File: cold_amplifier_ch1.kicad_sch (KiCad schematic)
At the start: 28 parts, among them J2 T1M-03-F-SV-L, J3 T1M-03-F-SV-L, J4 T1M-03-F-SV-L, J5 T1M-03-F-SV-L

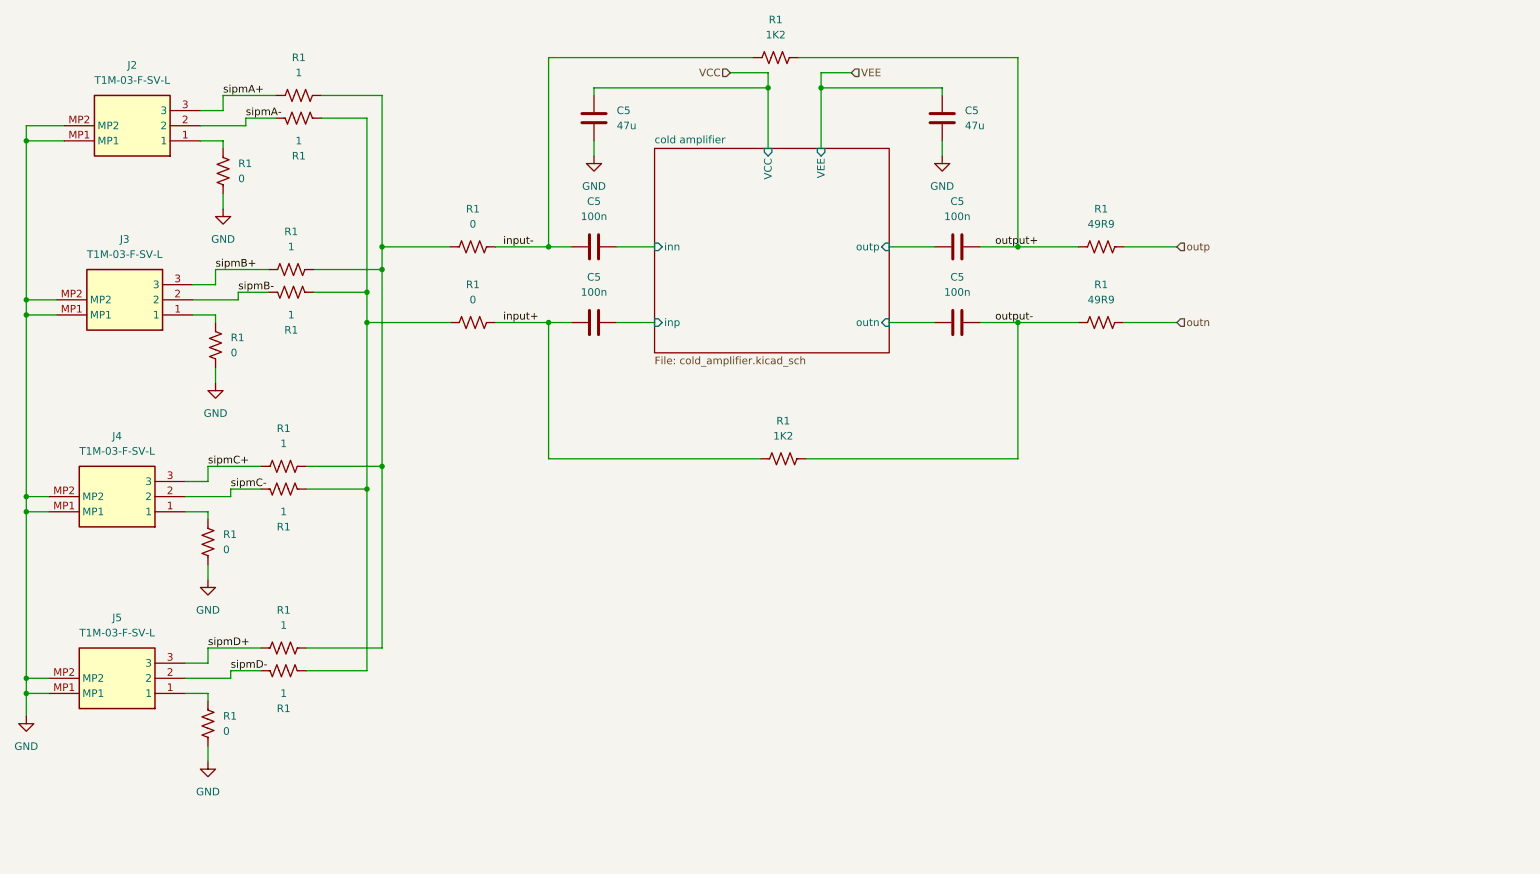
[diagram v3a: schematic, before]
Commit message: completed BOM list; replaced 47u with 33u capacitor
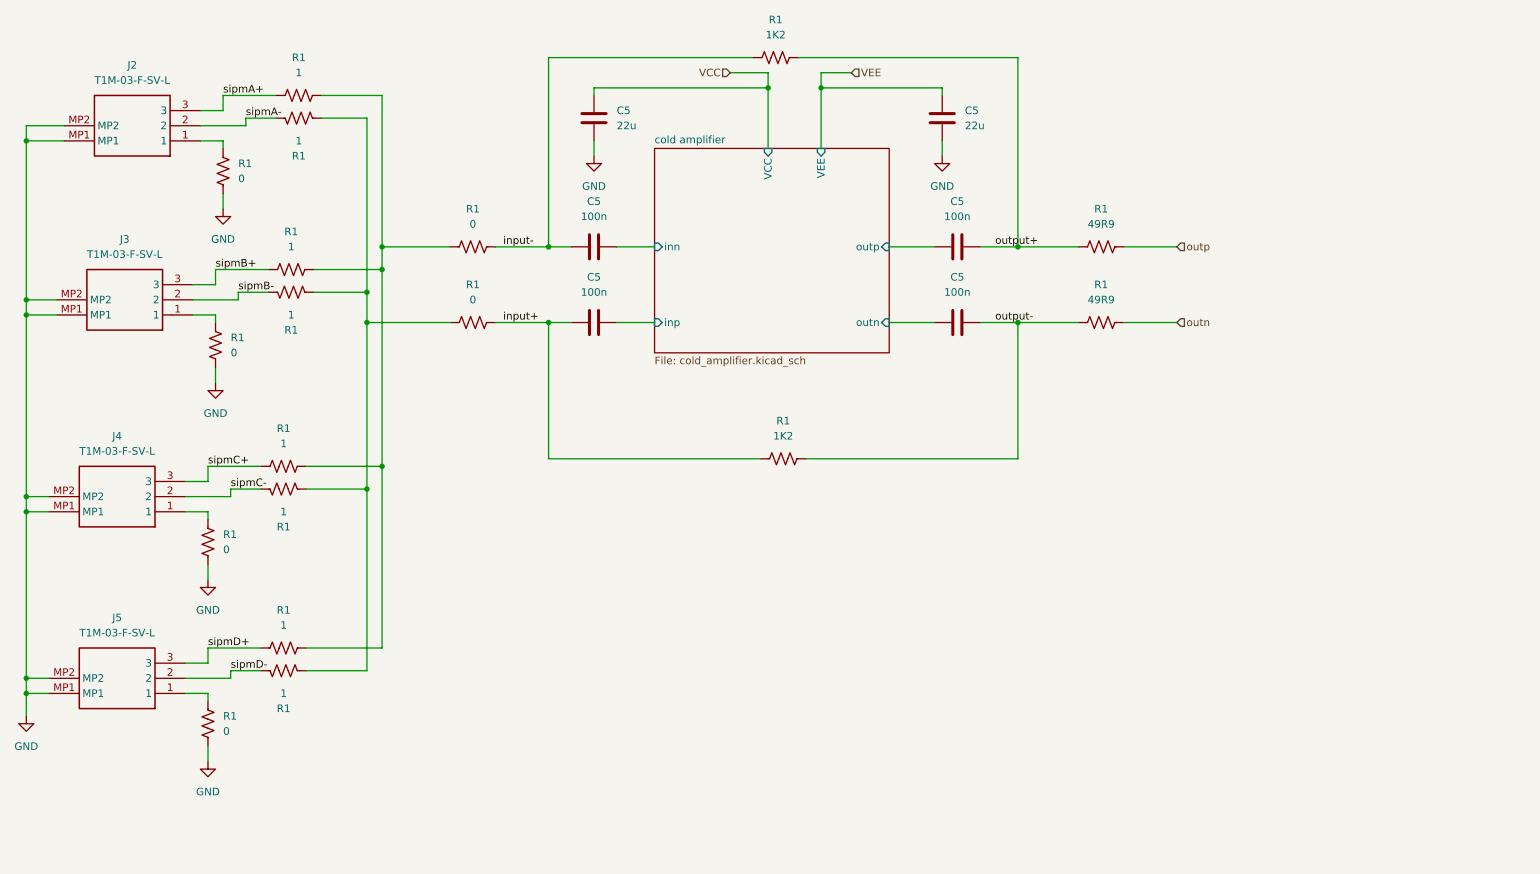
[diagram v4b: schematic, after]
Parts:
- C5: value 47u -> 22u; Digikey Part Number (none) -> 490-GRM31C5C1H224JE02LCT-ND; Manufacturer (none) -> Murata Electronics; Part Number (none) -> GRM31C5C1H224JE02L
- J2: Digikey Part SAM15301CT-ND -> (none); Digikey Part Number (none) -> SAM15301CT-ND; Height 5.5 -> (none); Manufacturer (none) -> SAMTEC; Manufacturer Name SAMTEC -> (none); Manufacturer_Name SAMTEC -> (none); Manufacturer_Part_Number T1M-03-F-SV-L -> (none); Mouser Part Number 200-T1M03FSVL -> (none); Mouser Price/Stock https://www.mouser.co.uk/ProductDetail/Samtec/T1M-03-F-SV-L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 -> (none)
- J3, J4, J5: Description  Connector Header Surface Mount 3 position 0.039" (1.00mm) -> (none); Height 5.5 -> (none); Manufacturer (none) -> SAMTEC; Manufacturer Name SAMTEC -> (none); Manufacturer_Name SAMTEC -> (none); Manufacturer_Part_Number T1M-03-F-SV-L -> (none); Mouser Part Number 200-T1M03FSVL -> (none); Mouser Price/Stock https://www.mouser.co.uk/ProductDetail/Samtec/T1M-03-F-SV-L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 -> (none)
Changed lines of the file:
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@@
       (effects (font (size 1.27 1.27)) (justify left top) hide)
     )
-    (property "Datasheet" "http://suddendocs.samtec.com/prints/t1m-xx-x-sv-l-x-mkt.pdf" (at 25.4 -28.55 0)
-      (effects (font (size 1.27 1.27)) (justify left top) hide)
-    )
-    (property "Height" "5.5" (at 25.4 -228.55 0)
-      (effects (font (size 1.27 1.27)) (justify left top) hide)
-    )
-    (property "Mouser Part Number" "200-T1M03FSVL" (at 25.4 -328.55 0)
-      (effects (font (size 1.27 1.27)) (justify left top) hide)
-    )
-    (property "Mouser Price/Stock" "https://www.mouser.co.uk/ProductDetail/Samtec/T1M-03-F-SV-L?qs=PB6%2FjmICvI1GeF9c7xI%252BBQ%3D%3D" (at 25.4 -428.55 0)
-      (effects (font (size 1.27 1.27)) (justify left top) hide)
-    )
-    (property "Manufacturer_Name" "SAMTEC" (at 25.4 -528.55 0)
-      (effects (font (size 1.27 1.27)) (justify left top) hide)
-    )
-    (property "Manufacturer_Part_Number" "T1M-03-F-SV-L" (at 25.4 -628.55 0)
-      (effects (font (size 1.27 1.27)) (justify left top) hide)
-    )
-    (property "Manufacturer Name" "SAMTEC" (at 25.4 -528.55 0)
+    (property "Datasheet" "" (at 25.4 -28.55 0)
+      (effects (font (size 1.27 1.27)) (justify left top) hide)
+    )
+    (property "Manufacturer" "SAMTEC" (at 25.4 -528.55 0)
       (effects (font (size 1.27 1.27)) (justify left top) hide)
     )
@@
     )
     (property "Digikey Part Number" "SAM15301CT-ND" (at 33.02 157.48 0)
-      (effects (font (size 1.27 1.27)) hide)
-    )
-    (property "Description " "Connector Header Surface Mount 3 position 0.039\" (1.00mm)" (at 41.91 176.53 0)
       (effects (font (size 1.27 1.27)) hide)
     )
@@
       (effects (font (size 1.27 1.27)) (justify left top) hide)
     )
-    (property "Datasheet" "http://suddendocs.samtec.com/prints/t1m-xx-x-sv-l-x-mkt.pdf" (at 25.4 -59.03 0)
-      (effects (font (size 1.27 1.27)) (justify left top) hide)
-    )
-    (property "Height" "5.5" (at 25.4 -259.03 0)
-      (effects (font (size 1.27 1.27)) (justify left top) hide)
-    )
-    (property "Mouser Part Number" "200-T1M03FSVL" (at 25.4 -359.03 0)
-      (effects (font (size 1.27 1.27)) (justify left top) hide)
-    )
-    (property "Mouser Price/Stock" "https://www.mouser.co.uk/ProductDetail/Samtec/T1M-03-F-SV-L?qs=PB6%2FjmICvI1GeF9c7xI%252BBQ%3D%3D" (at 25.4 -459.03 0)
-      (effects (font (size 1.27 1.27)) (justify left top) hide)
-    )
-    (property "Manufacturer_Name" "SAMTEC" (at 25.4 -559.03 0)
-      (effects (font (size 1.27 1.27)) (justify left top) hide)
-    )
-    (property "Manufacturer_Part_Number" "T1M-03-F-SV-L" (at 25.4 -659.03 0)
-      (effects (font (size 1.27 1.27)) (justify left top) hide)
-    )
-    (property "Manufacturer Name" "SAMTEC" (at 25.4 -559.03 0)
+    (property "Datasheet" "" (at 25.4 -59.03 0)
+      (effects (font (size 1.27 1.27)) (justify left top) hide)
+    )
+    (property "Manufacturer" "SAMTEC" (at 25.4 -559.03 0)
       (effects (font (size 1.27 1.27)) (justify left top) hide)
     )
@@
     )
     (property "Digikey Part Number" "SAM15301CT-ND" (at 33.02 127 0)
-      (effects (font (size 1.27 1.27)) hide)
-    )
-    (property "Description " "Connector Header Surface Mount 3 position 0.039\" (1.00mm)" (at 41.91 146.05 0)
       (effects (font (size 1.27 1.27)) hide)
     )
@@
       (effects (font (size 1.27 1.27)) (justify left top) hide)
     )
-    (property "Datasheet" "http://suddendocs.samtec.com/prints/t1m-xx-x-sv-l-x-mkt.pdf" (at 26.67 -92.05 0)
-      (effects (font (size 1.27 1.27)) (justify left top) hide)
-    )
-    (property "Height" "5.5" (at 26.67 -292.05 0)
-      (effects (font (size 1.27 1.27)) (justify left top) hide)
-    )
-    (property "Mouser Part Number" "200-T1M03FSVL" (at 26.67 -392.05 0)
-      (effects (font (size 1.27 1.27)) (justify left top) hide)
-    )
-    (property "Mouser Price/Stock" "https://www.mouser.co.uk/ProductDetail/Samtec/T1M-03-F-SV-L?qs=PB6%2FjmICvI1GeF9c7xI%252BBQ%3D%3D" (at 26.67 -492.05 0)
-      (effects (font (size 1.27 1.27)) (justify left top) hide)
-    )
-    (property "Manufacturer_Name" "SAMTEC" (at 26.67 -592.05 0)
-      (effects (font (size 1.27 1.27)) (justify left top) hide)
-    )
-    (property "Manufacturer_Part_Number" "T1M-03-F-SV-L" (at 26.67 -692.05 0)
-      (effects (font (size 1.27 1.27)) (justify left top) hide)
-    )
-    (property "Manufacturer Name" "SAMTEC" (at 26.67 -592.05 0)
+    (property "Datasheet" "" (at 26.67 -92.05 0)
+      (effects (font (size 1.27 1.27)) (justify left top) hide)
+    )
+    (property "Manufacturer" "SAMTEC" (at 26.67 -592.05 0)
       (effects (font (size 1.27 1.27)) (justify left top) hide)
     )
@@
     )
     (property "Digikey Part Number" "SAM15301CT-ND" (at 34.29 93.98 0)
-      (effects (font (size 1.27 1.27)) hide)
-    )
-    (property "Description " "Connector Header Surface Mount 3 position 0.039\" (1.00mm)" (at 43.18 113.03 0)
       (effects (font (size 1.27 1.27)) hide)
     )
@@
       (effects (font (size 1.27 1.27)) (justify left top) hide)
     )
-    (property "Datasheet" "http://suddendocs.samtec.com/prints/t1m-xx-x-sv-l-x-mkt.pdf" (at 27.94 -121.26 0)
-      (effects (font (size 1.27 1.27)) (justify left top) hide)
-    )
-    (property "Height" "5.5" (at 27.94 -321.26 0)
-      (effects (font (size 1.27 1.27)) (justify left top) hide)
-    )
-    (property "Mouser Part Number" "200-T1M03FSVL" (at 27.94 -421.26 0)
-      (effects (font (size 1.27 1.27)) (justify left top) hide)
-    )
-    (property "Mouser Price/Stock" "https://www.mouser.co.uk/ProductDetail/Samtec/T1M-03-F-SV-L?qs=PB6%2FjmICvI1GeF9c7xI%252BBQ%3D%3D" (at 27.94 -521.26 0)
-      (effects (font (size 1.27 1.27)) (justify left top) hide)
-    )
-    (property "Manufacturer_Name" "SAMTEC" (at 27.94 -621.26 0)
-      (effects (font (size 1.27 1.27)) (justify left top) hide)
-    )
-    (property "Manufacturer_Part_Number" "T1M-03-F-SV-L" (at 27.94 -721.26 0)
-      (effects (font (size 1.27 1.27)) (justify left top) hide)
-    )
-    (property "Manufacturer Name" "SAMTEC" (at 27.94 -621.26 0)
+    (property "Datasheet" "" (at 27.94 -121.26 0)
+      (effects (font (size 1.27 1.27)) (justify left top) hide)
+    )
+    (property "Manufacturer" "SAMTEC" (at 27.94 -621.26 0)
       (effects (font (size 1.27 1.27)) (justify left top) hide)
     )
@@
       (effects (font (size 1.27 1.27)) (justify left top) hide)
     )
-    (property "Digikey Part" "SAM15301CT-ND" (at 46.99 73.66 0)
-      (effects (font (size 1.27 1.27)) hide)
-    )
-    (property "Description" "Connector Header Surface Mount 3 position 0.039\" (1.00mm)" (at 46.99 73.66 0)
+    (property "Digikey Part Number" "SAM15301CT-ND" (at 35.56 64.77 0)
       (effects (font (size 1.27 1.27)) hide)
     )
@@
       (effects (font (size 1.27 1.27)) (justify right))
     )
-    (property "Value" "47u" (at 175.26 71.12 0)
+    (property "Value" "22u" (at 175.26 71.12 0)
       (effects (font (size 1.27 1.27)) (justify right))
     )
@@
       (effects (font (size 1.27 1.27)) hide)
     )
-    (property "Manufacturer" "" (at 171.45 69.85 0)
-      (effects (font (size 1.27 1.27)) hide)
-    )
-    (property "Part Number" "" (at 171.45 69.85 0)
-      (effects (font (size 1.27 1.27)) hide)
-    )
-    (property "Digikey Part Number" "" (at 171.45 69.85 0)
-      (effects (font (size 1.27 1.27)) hide)
-    )
-    (property "Description" "" (at 171.45 69.85 0)
+    (property "Manufacturer" "Murata Electronics" (at 171.45 69.85 0)
+      (effects (font (size 1.27 1.27)) hide)
+    )
+    (property "Part Number" "GRM31C5C1H224JE02L" (at 171.45 69.85 0)
+      (effects (font (size 1.27 1.27)) hide)
+    )
+    (property "Digikey Part Number" "490-GRM31C5C1H224JE02LCT-ND" (at 171.45 69.85 0)
+      (effects (font (size 1.27 1.27)) hide)
+    )
+    (property "Description" "0.22 µF ±5% 50V Ceramic Capacitor C0G, NP0 1206 (3216 Metric)" (at 171.45 69.85 0)
       (effects (font (size 1.27 1.27)) hide)
     )
@@
       (effects (font (size 1.27 1.27)) (justify right))
     )
-    (property "Value" "47u" (at 116.84 71.12 0)
+    (property "Value" "22u" (at 116.84 71.12 0)
       (effects (font (size 1.27 1.27)) (justify right))
     )
@@
       (effects (font (size 1.27 1.27)) hide)
     )
-    (property "Manufacturer" "" (at 113.03 69.85 0)
-      (effects (font (size 1.27 1.27)) hide)
-    )
-    (property "Part Number" "" (at 113.03 69.85 0)
-      (effects (font (size 1.27 1.27)) hide)
-    )
-    (property "Digikey Part Number" "" (at 113.03 69.85 0)
-      (effects (font (size 1.27 1.27)) hide)
-    )
-    (property "Description" "" (at 113.03 69.85 0)
-      (effects (font (size 1.27 1.27)) hide)
-    )
+    (property "Manufacturer" "Murata Electronics" (at 113.03 69.85 0)
+      (effects (font (size 1.27 1.27)) hide)
+    )
+    (property "Part Number" "GRM31C5C1H224JE02L" (at 113.03 69.85 0)
+      (effects (font (size 1.27 1.27)) hide)
+    )
+    (property "Digikey Part Number" "490-GRM31C5C1H224JE02LCT-ND" (at 113.03 69.85 0)
+      (effects (font (size 1.27 1.27)) hide)
+    )
+    (property "Description" "0.22 µF ±5% 50V Ceramic Capacitor C0G, NP0 1206 (3216 Metric)" (at 113.03 69.85 0)
+      (effects (font (size 1.27 1.27)) hide)
+    )

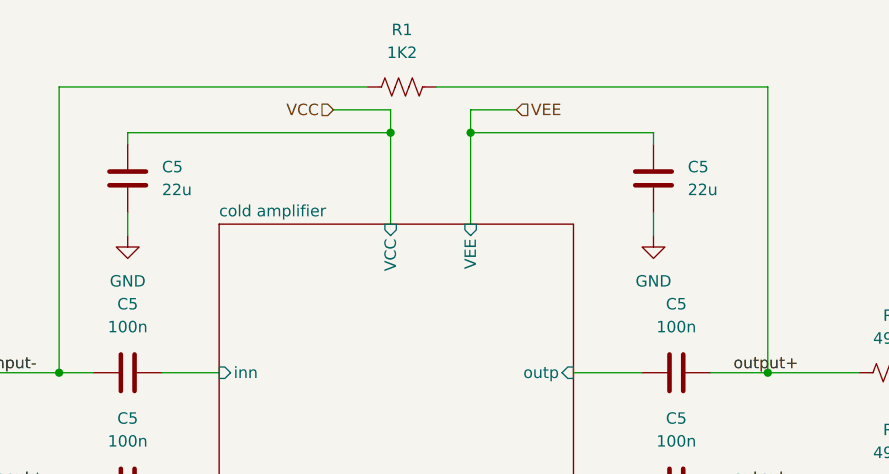
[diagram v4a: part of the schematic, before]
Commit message: Changed footprint to removed unused silkscreen symbols; silkscreen more legible; changed texts next to arrows; changed wrong 0.22u cap to 47u
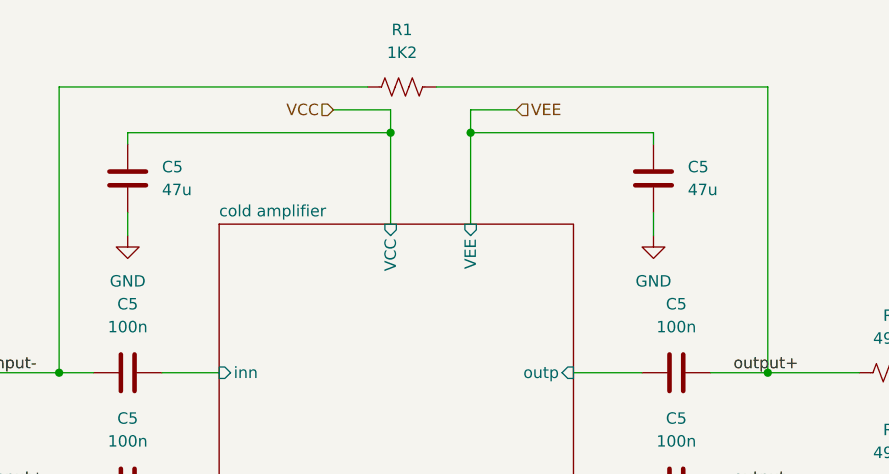
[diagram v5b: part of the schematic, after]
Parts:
- C5: value 22u -> 47u; Digikey Part Number 490-GRM31C5C1H224JE02LCT-ND -> 445-8047-1-ND; Manufacturer Murata Electronics -> TDK Corporation; Part Number GRM31C5C1H224JE02L -> C3216X5R1E476M160AC
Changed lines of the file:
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@@
       (effects (font (size 1.27 1.27)) (justify right))
     )
-    (property "Value" "22u" (at 175.26 71.12 0)
+    (property "Value" "47u" (at 175.26 71.12 0)
       (effects (font (size 1.27 1.27)) (justify right))
     )
@@
       (effects (font (size 1.27 1.27)) hide)
     )
-    (property "Manufacturer" "Murata Electronics" (at 171.45 69.85 0)
+    (property "Manufacturer" "TDK Corporation" (at 171.45 69.85 0)
       (effects (font (size 1.27 1.27)) hide)
     )
-    (property "Part Number" "GRM31C5C1H224JE02L" (at 171.45 69.85 0)
+    (property "Part Number" "C3216X5R1E476M160AC" (at 171.45 69.85 0)
       (effects (font (size 1.27 1.27)) hide)
     )
-    (property "Digikey Part Number" "490-GRM31C5C1H224JE02LCT-ND" (at 171.45 69.85 0)
+    (property "Digikey Part Number" "445-8047-1-ND" (at 171.45 69.85 0)
       (effects (font (size 1.27 1.27)) hide)
     )
-    (property "Description" "0.22 µF ±5% 50V Ceramic Capacitor C0G, NP0 1206 (3216 Metric)" (at 171.45 69.85 0)
+    (property "Description" "47 µF ±20% 25V Ceramic Capacitor X5R 1206 (3216 Metric)" (at 171.45 69.85 0)
       (effects (font (size 1.27 1.27)) hide)
     )
@@
       (effects (font (size 1.27 1.27)) (justify right))
     )
-    (property "Value" "22u" (at 116.84 71.12 0)
+    (property "Value" "47u" (at 116.84 71.12 0)
       (effects (font (size 1.27 1.27)) (justify right))
     )
@@
       (effects (font (size 1.27 1.27)) hide)
     )
-    (property "Manufacturer" "Murata Electronics" (at 113.03 69.85 0)
+    (property "Manufacturer" "TDK Corporation" (at 113.03 69.85 0)
       (effects (font (size 1.27 1.27)) hide)
     )
-    (property "Part Number" "GRM31C5C1H224JE02L" (at 113.03 69.85 0)
+    (property "Part Number" "C3216X5R1E476M160AC" (at 113.03 69.85 0)
       (effects (font (size 1.27 1.27)) hide)
     )
-    (property "Digikey Part Number" "490-GRM31C5C1H224JE02LCT-ND" (at 113.03 69.85 0)
+    (property "Digikey Part Number" "445-8047-1-ND" (at 113.03 69.85 0)
       (effects (font (size 1.27 1.27)) hide)
     )
-    (property "Description" "0.22 µF ±5% 50V Ceramic Capacitor C0G, NP0 1206 (3216 Metric)" (at 113.03 69.85 0)
+    (property "Description" "47 µF ±20% 25V Ceramic Capacitor X5R 1206 (3216 Metric)" (at 113.03 69.85 0)
       (effects (font (size 1.27 1.27)) hide)
     )
